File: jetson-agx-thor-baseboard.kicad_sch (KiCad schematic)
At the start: 7 parts

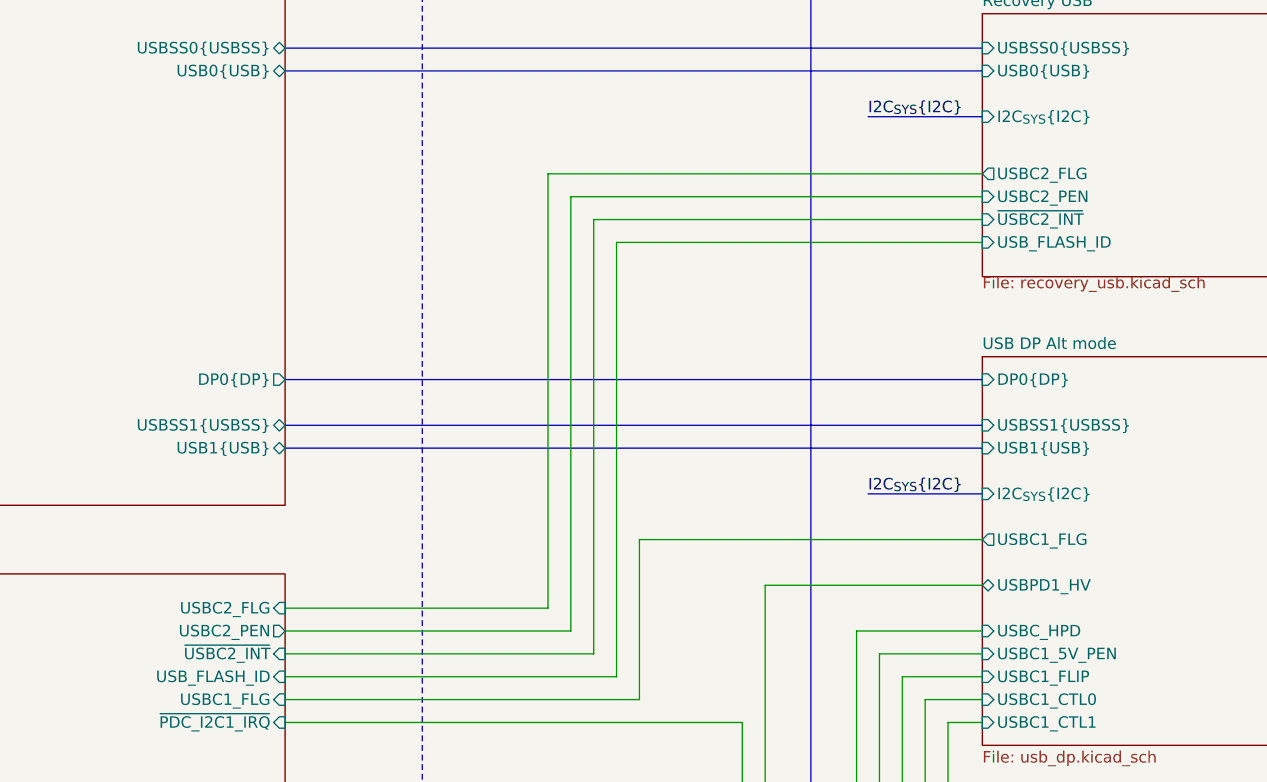
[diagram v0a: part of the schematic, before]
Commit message: [#85326] Fix USB-C 2 ID and enable handling
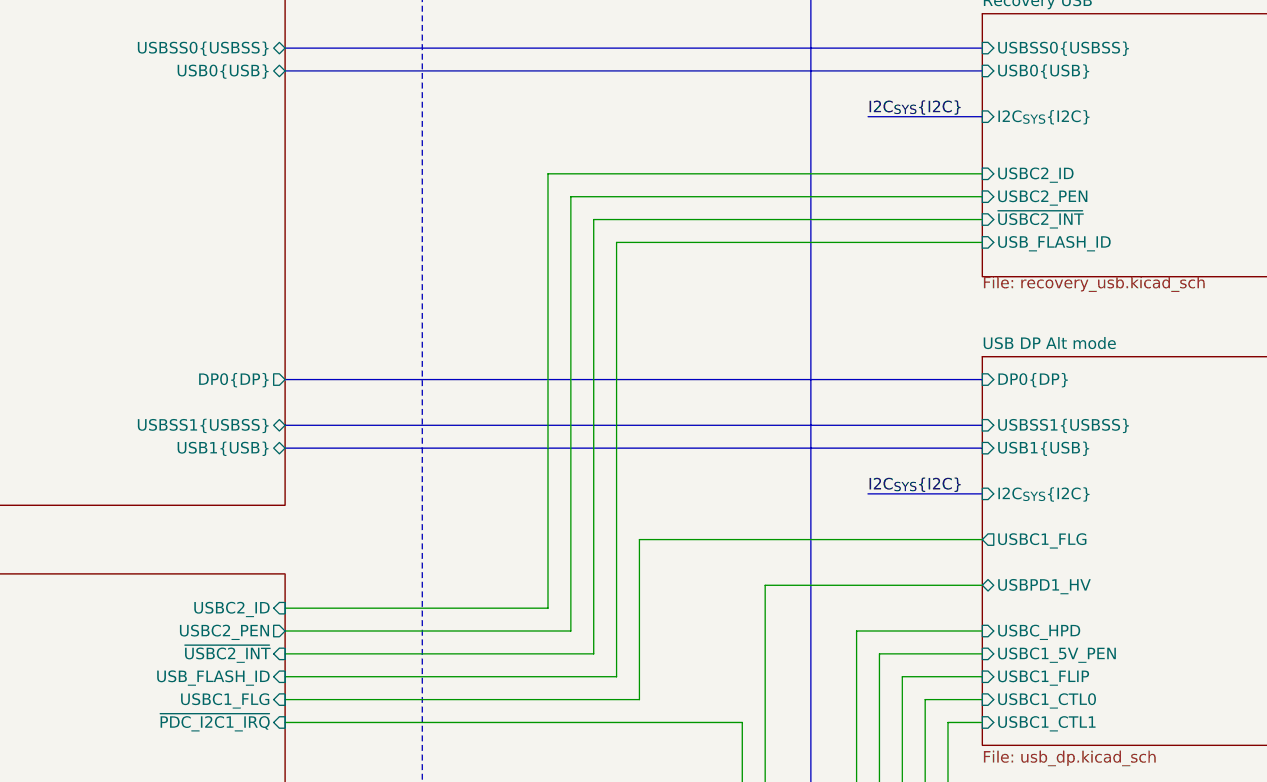
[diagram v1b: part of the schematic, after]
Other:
- sheet Recovery USB ports: added USBC2_ID; removed USBC2_FLG
- sheet SoM_IO ports: added USBC2_ID; removed USBC2_FLG
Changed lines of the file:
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@@
-			)
-		)
-		(pin "USBC2_FLG" input
-			(at 254 135.89 0)
-			(effects
-				(font
-					(size 1.27 1.27)
-				)
-				(justify right)
 			)
 		)
@@
 				)
 				(justify left)
+			)
+		)
+		(pin "USBC2_ID" input
+			(at 254 135.89 0)
+			(effects
+				(font
+					(size 1.27 1.27)
+				)
+				(justify right)
 			)
 		)
@@
 			)
 		)
-		(pin "USBC2_FLG" output
-			(at 331.47 87.63 180)
-			(effects
-				(font
-					(size 1.27 1.27)
-				)
-				(justify left)
-			)
-		)
 		(pin "USBC2_PEN" input
 			(at 331.47 90.17 180)
@@
 			(effects
 				(font
+					(size 1.27 1.27)
+				)
+				(justify left)
+			)
+		)
+		(pin "USBC2_ID" input
+			(at 331.47 87.63 180)
+			(effects
+				(font

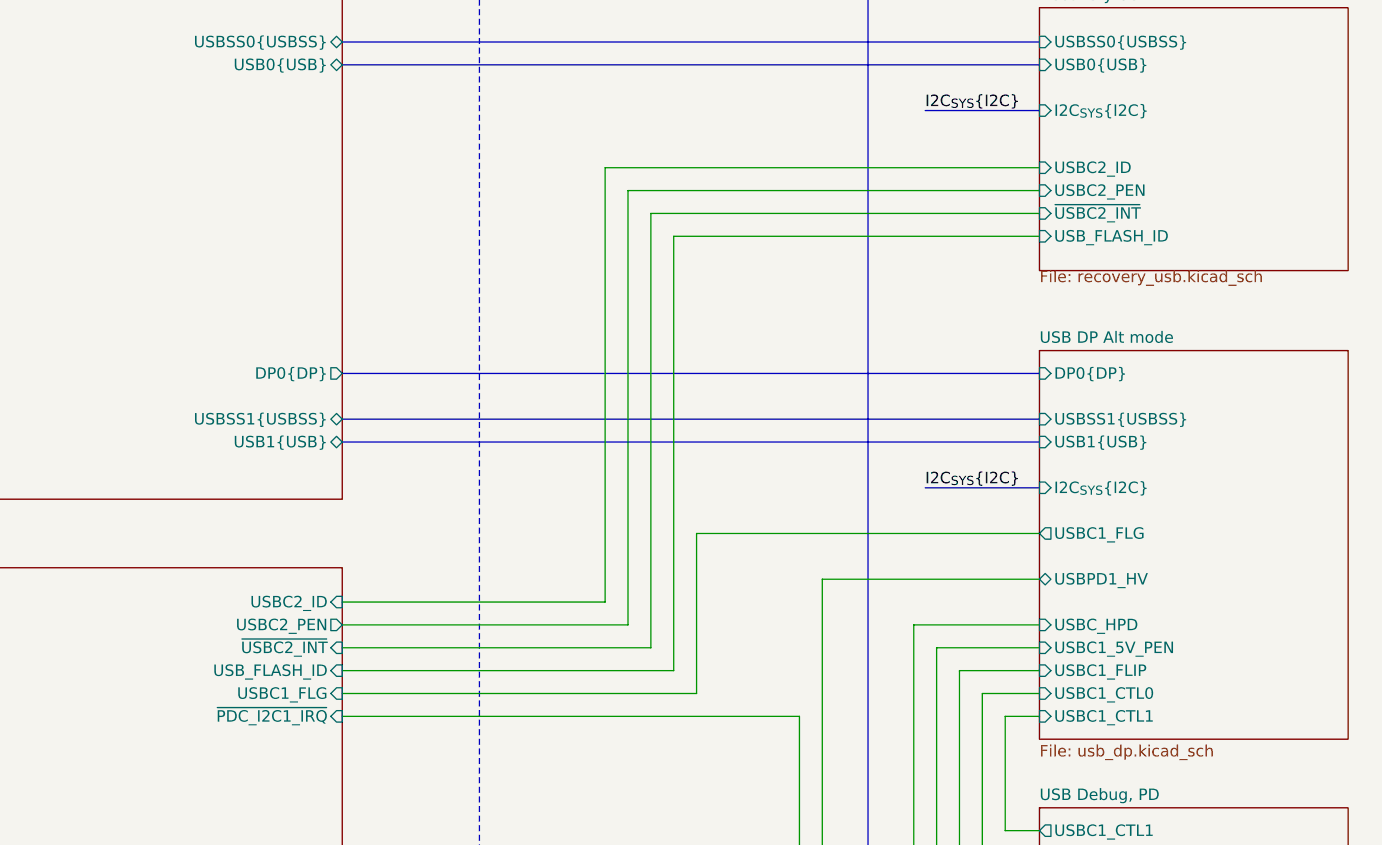
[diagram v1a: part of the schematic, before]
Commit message: [#85326] Improved USB-C 2 control signal connections
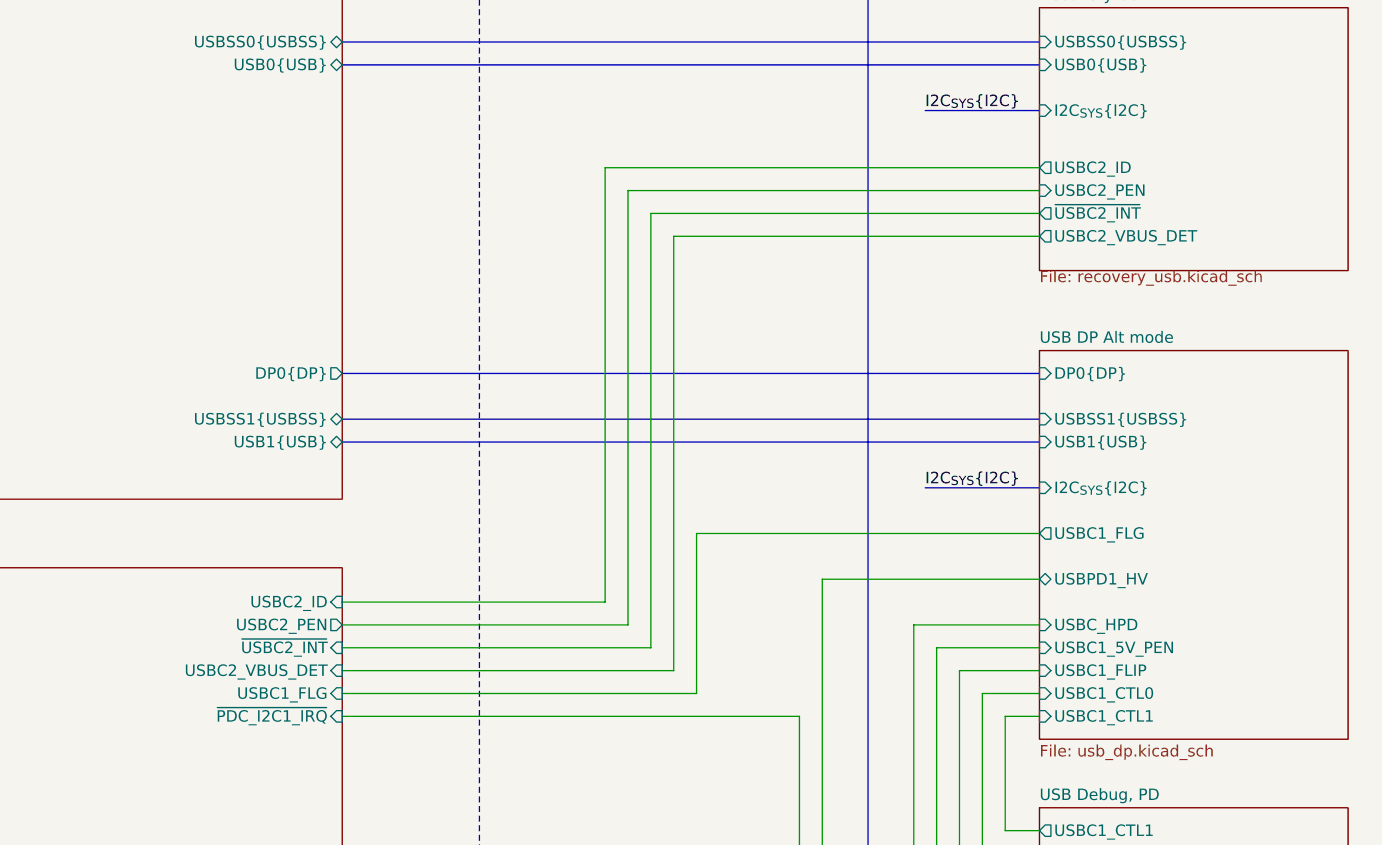
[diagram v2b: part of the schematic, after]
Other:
- sheet Recovery USB ports: added USBC2_VBUS_DET; removed USB_FLASH_ID
- sheet SoM_IO ports: added USBC2_VBUS_DET; removed USB_FLASH_ID
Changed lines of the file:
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@@
-			)
-		)
-		(pin "USB_FLASH_ID" input
-			(at 254 143.51 0)
-			(effects
-				(font
-					(size 1.27 1.27)
-				)
-				(justify right)
 			)
 		)
@@
 		(pin "USBC2_ID" input
 			(at 254 135.89 0)
+			(effects
+				(font
+					(size 1.27 1.27)
+				)
+				(justify right)
+			)
+		)
+		(pin "USBC2_VBUS_DET" input
+			(at 254 143.51 0)
 			(effects
 				(font
@@
 			)
 		)
-		(pin "USB_FLASH_ID" input
-			(at 331.47 95.25 180)
+		(pin "~{USBC2_INT}" output
+			(at 331.47 92.71 180)
+			(effects
+				(font
+					(size 1.27 1.27)
+				)
+				(justify left)
+			)
+		)
+		(pin "USBC2_ID" output
+			(at 331.47 87.63 180)
 			(effects
 				(font
@@
 			)
 		)
-		(pin "~{USBC2_INT}" input
-			(at 331.47 92.71 180)
-			(effects
-				(font
-					(size 1.27 1.27)
-				)
-				(justify left)
-			)
-		)
-		(pin "USBC2_ID" input
-			(at 331.47 87.63 180)
-			(effects
-				(font
+		(pin "USBC2_VBUS_DET" output
+			(at 331.47 95.25 180)
+			(effects
+				(font

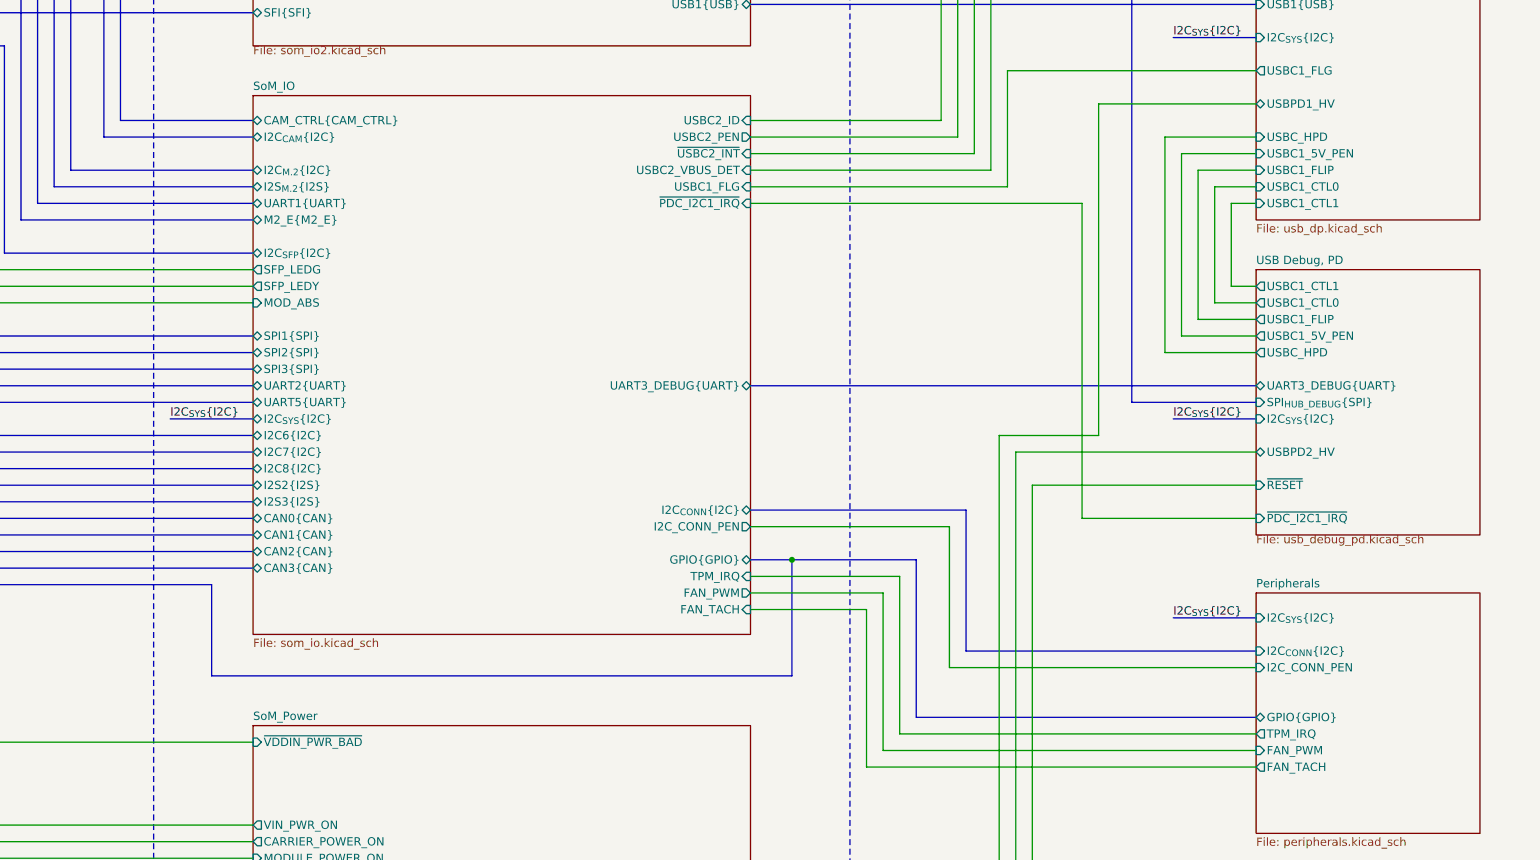
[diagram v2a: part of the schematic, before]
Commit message: [#85326] Fix Thor symbol, Free reserved GPIOs
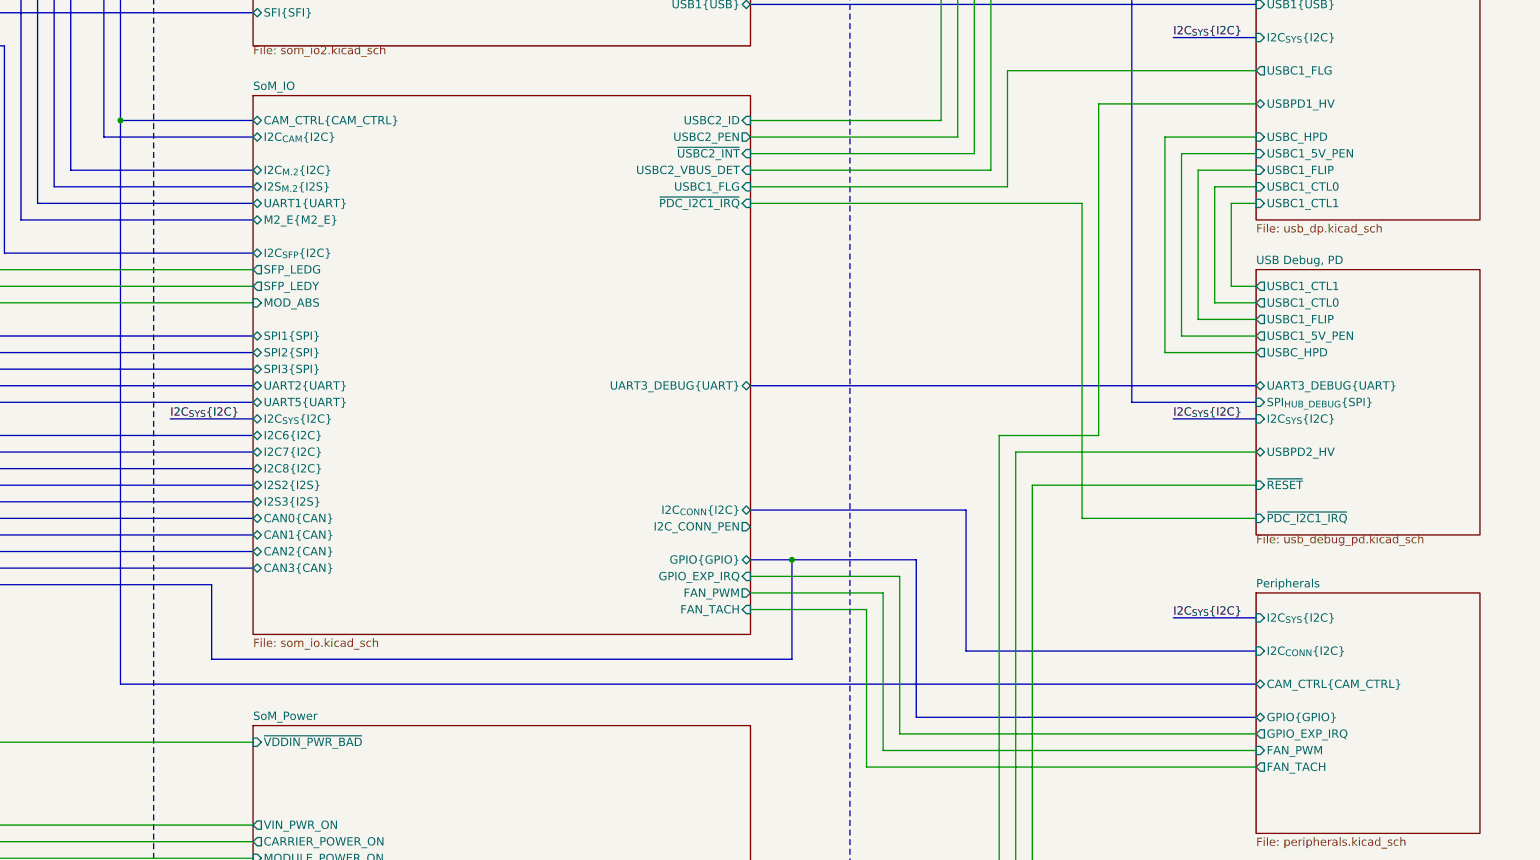
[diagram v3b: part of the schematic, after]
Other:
- sheet Peripherals ports: added CAM_CTRL{CAM_CTRL}, GPIO_EXP_IRQ; removed I2C_CONN_PEN, TPM_IRQ
- sheet SoM_IO ports: added GPIO_EXP_IRQ; removed TPM_IRQ
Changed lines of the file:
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@@
 	)
 	(junction
+		(at 157.48 135.89)
+		(diameter 0)
+		(color 0 0 0 0)
+	)
+	(junction
 		(at 381 245.11)
 		(diameter 0)
@@
 		)
 	)
-	(wire
+	(bus
 		(pts
-			(xy 381 245.11) (xy 382.27 245.11)
+			(xy 157.48 222.25) (xy 331.47 222.25)
 		)
 		(stroke
@@
 	(wire
 		(pts
-			(xy 331.47 166.37) (xy 322.58 166.37)
+			(xy 381 245.11) (xy 382.27 245.11)
 		)
 		(stroke
@@
 	(wire
 		(pts
-			(xy 304.8 196.85) (xy 304.8 148.59)
+			(xy 331.47 166.37) (xy 322.58 166.37)
 		)
 		(stroke
@@
 	(wire
 		(pts
-			(xy 254 198.12) (xy 284.48 198.12)
+			(xy 304.8 196.85) (xy 304.8 148.59)
 		)
 		(stroke
@@
 	(wire
 		(pts
-			(xy 284.48 219.71) (xy 331.47 219.71)
-		)
-		(stroke
-			(width 0)
-			(type default)
-		)
-	)
-	(wire
-		(pts
 			(xy 294.64 267.97) (xy 294.64 186.69)
 		)
@@
 		)
 	)
-	(wire
-		(pts
-			(xy 284.48 219.71) (xy 284.48 198.12)
-		)
-		(stroke
-			(width 0)
-			(type default)
-		)
-	)
 	(bus
 		(pts
@@
 	(bus
 		(pts
-			(xy 171.45 220.98) (xy 171.45 207.01)
+			(xy 171.45 218.44) (xy 171.45 207.01)
+		)
+		(stroke
+			(width 0)
+			(type default)
+		)
+	)
+	(wire
+		(pts
+			(xy 254 205.74) (xy 276.86 205.74)
 		)
 		(stroke
@@
 		)
 	)
-	(wire
+	(bus
 		(pts
-			(xy 254 205.74) (xy 276.86 205.74)
+			(xy 124.46 153.67) (xy 100.33 153.67)
 		)
 		(stroke
 			(width 0)
 			(type default)
+			(color 132 0 0 1)
 		)
 	)
-	(bus
+	(wire
 		(pts
-			(xy 124.46 153.67) (xy 100.33 153.67)
+			(xy 276.86 229.87) (xy 331.47 229.87)
 		)
 		(stroke
 			(width 0)
 			(type default)
-			(color 132 0 0 1)
 		)
 	)
@@
 	(wire
 		(pts
+			(xy 276.86 205.74) (xy 276.86 229.87)
+		)
+		(stroke
+			(width 0)
+			(type default)
+		)
+	)
+	(wire
+		(pts
 			(xy 381 213.36) (xy 382.27 213.36)
 		)
@@
 	(bus
 		(pts
-			(xy 260.35 220.98) (xy 171.45 220.98)
+			(xy 157.48 135.89) (xy 157.48 222.25)
+		)
+		(stroke
+			(width 0)
+			(type default)
+		)
+	)
+	(bus
+		(pts
+			(xy 260.35 218.44) (xy 171.45 218.44)
 		)
 		(stroke
@@
 	(bus
 		(pts
-			(xy 260.35 203.2) (xy 260.35 220.98)
+			(xy 260.35 203.2) (xy 260.35 218.44)
 		)
 		(stroke
@@
 		)
 	)
-	(wire
-		(pts
-			(xy 276.86 229.87) (xy 331.47 229.87)
-		)
-		(stroke
-			(width 0)
-			(type default)
-		)
-	)
 	(bus
 		(pts
@@
 	(wire
 		(pts
-			(xy 276.86 205.74) (xy 276.86 229.87)
-		)
-		(stroke
-			(width 0)
-			(type default)
-		)
-	)
-	(wire
-		(pts
 			(xy 331.47 161.29) (xy 327.66 161.29)
 		)
@@
 			)
 		)
-		(pin "TPM_IRQ" input
-			(at 254 205.74 0)
-			(effects
-				(font
-					(size 1.27 1.27)
-				)
-				(justify right)
-			)
-		)
 		(pin "GPIO{GPIO}" bidirectional
 			(at 254 203.2 0)
@@
 			)
 		)
+		(pin "GPIO_EXP_IRQ" input
+			(at 254 205.74 0)
+			(effects
+				(font
+					(size 1.27 1.27)
+				)
+				(justify right)
+			)
+		)
 		(instances
 			(project "jetson-agx-thor-baseboard"
@@
 			)
 		)
-		(pin "I2C_CONN_PEN" input
-			(at 331.47 219.71 180)
+		(pin "I2C_{CONN}{I2C}" input
+			(at 331.47 217.17 180)
 			(effects
 				(font
@@
 			)
 		)
-		(pin "I2C_{CONN}{I2C}" input
-			(at 331.47 217.17 180)
+		(pin "I2C_{SYS}{I2C}" input
+			(at 331.47 212.09 180)
 			(effects
 				(font
@@
 			)
 		)
-		(pin "I2C_{SYS}{I2C}" input
-			(at 331.47 212.09 180)
+		(pin "CAM_CTRL{CAM_CTRL}" bidirectional
+			(at 331.47 222.25 180)
 			(effects
 				(font
@@
 			)
 		)
-		(pin "TPM_IRQ" output
+		(pin "GPIO_EXP_IRQ" output
 			(at 331.47 229.87 180)
 			(effects

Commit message: [#85488] Sync sch branches
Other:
- sheet DCDC ports: added CARRIER_PWR_ON; removed none
- sheet Power ports: added ~{VDDIN_PWR_BAD}; removed CARRIER_POWER_ON, MODULE_POWER_ON
- sheet SoM_Power ports: added CARRIER_PWR_ON; removed CARRIER_POWER_ON, MODULE_POWER_ON
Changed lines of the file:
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@@
 	)
 	(junction
+		(at 107.95 246.38)
+		(diameter 0)
+		(color 0 0 0 0)
+	)
+	(junction
 		(at 116.84 88.9)
 		(diameter 0)
@@
 		)
 	)
+	(wire
+		(pts
+			(xy 110.49 228.6) (xy 110.49 241.3)
+		)
+		(stroke
+			(width 0)
+			(type default)
+		)
+	)
 	(bus
 		(pts
@@
 	(wire
 		(pts
-			(xy 100.33 231.14) (xy 177.8 231.14)
+			(xy 100.33 231.14) (xy 107.95 231.14)
+		)
+		(stroke
+			(width 0)
+			(type default)
+		)
+	)
+	(wire
+		(pts
+			(xy 107.95 246.38) (xy 177.8 246.38)
 		)
 		(stroke
@@
 	(wire
 		(pts
+			(xy 107.95 231.14) (xy 107.95 246.38)
+		)
+		(stroke
+			(width 0)
+			(type default)
+		)
+	)
+	(wire
+		(pts
 			(xy 116.84 270.51) (xy 297.18 270.51)
 		)
@@
 	(wire
 		(pts
-			(xy 100.33 248.92) (xy 177.8 248.92)
-		)
-		(stroke
-			(width 0)
-			(type default)
-		)
-	)
-	(wire
-		(pts
 			(xy 254 210.82) (xy 271.78 210.82)
 		)
@@
 	(wire
 		(pts
-			(xy 100.33 246.38) (xy 177.8 246.38)
+			(xy 100.33 246.38) (xy 107.95 246.38)
 		)
 		(stroke
@@
 		)
 	)
+	(wire
+		(pts
+			(xy 100.33 228.6) (xy 110.49 228.6)
+		)
+		(stroke
+			(width 0)
+			(type default)
+		)
+	)
 	(bus
 		(pts
@@
 		)
 	)
+	(wire
+		(pts
+			(xy 110.49 241.3) (xy 177.8 241.3)
+		)
+		(stroke
+			(width 0)
+			(type default)
+		)
+	)
 	(image
 		(at 59.2091 270)
@@
 			)
 		)
-		(pin "CARRIER_POWER_ON" input
-			(at 100.33 246.38 0)
-			(effects
-				(font
-					(size 1.27 1.27)
-				)
-				(justify right)
-			)
-		)
-		(pin "MODULE_POWER_ON" output
-			(at 100.33 248.92 0)
+		(pin "VIN_PWR_ON" input
+			(at 100.33 243.84 0)
 			(effects
 				(font
@@
 			)
 		)
-		(pin "VIN_PWR_ON" input
-			(at 100.33 243.84 0)
+		(pin "~{VDDIN_PWR_BAD}" output
+			(at 100.33 246.38 0)
 			(effects
 				(font
@@
 			)
 		)
+		(pin "CARRIER_PWR_ON" input
+			(at 100.33 228.6 0)
+			(effects
+				(font
+					(size 1.27 1.27)
+				)
+				(justify right)
+			)
+		)
 		(instances
 			(project "jetson-agx-thor-baseboard"
@@
 			)
 		)
-		(pin "CARRIER_POWER_ON" output
+		(pin "~{VDDIN_PWR_BAD}" input
 			(at 177.8 246.38 180)
 			(effects
@@
 			)
 		)
-		(pin "MODULE_POWER_ON" input
-			(at 177.8 248.92 180)
-			(effects
-				(font
-					(size 1.27 1.27)
-				)
-				(justify left)
-			)
-		)
-		(pin "~{VDDIN_PWR_BAD}" input
-			(at 177.8 231.14 180)
+		(pin "VIN_PWR_ON" output
+			(at 177.8 243.84 180)
 			(effects
 				(font
@@
 			)
 		)
-		(pin "VIN_PWR_ON" output
-			(at 177.8 243.84 180)
+		(pin "CARRIER_PWR_ON" output
+			(at 177.8 241.3 180)
 			(effects
 				(font
